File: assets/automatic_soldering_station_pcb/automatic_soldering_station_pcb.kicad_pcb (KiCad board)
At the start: 2 copper layers, 130 x 100 mm, 24 parts, among them J1 XY_MOS, J2 MAX6675, J3 MAX6675, J4 MAX6675

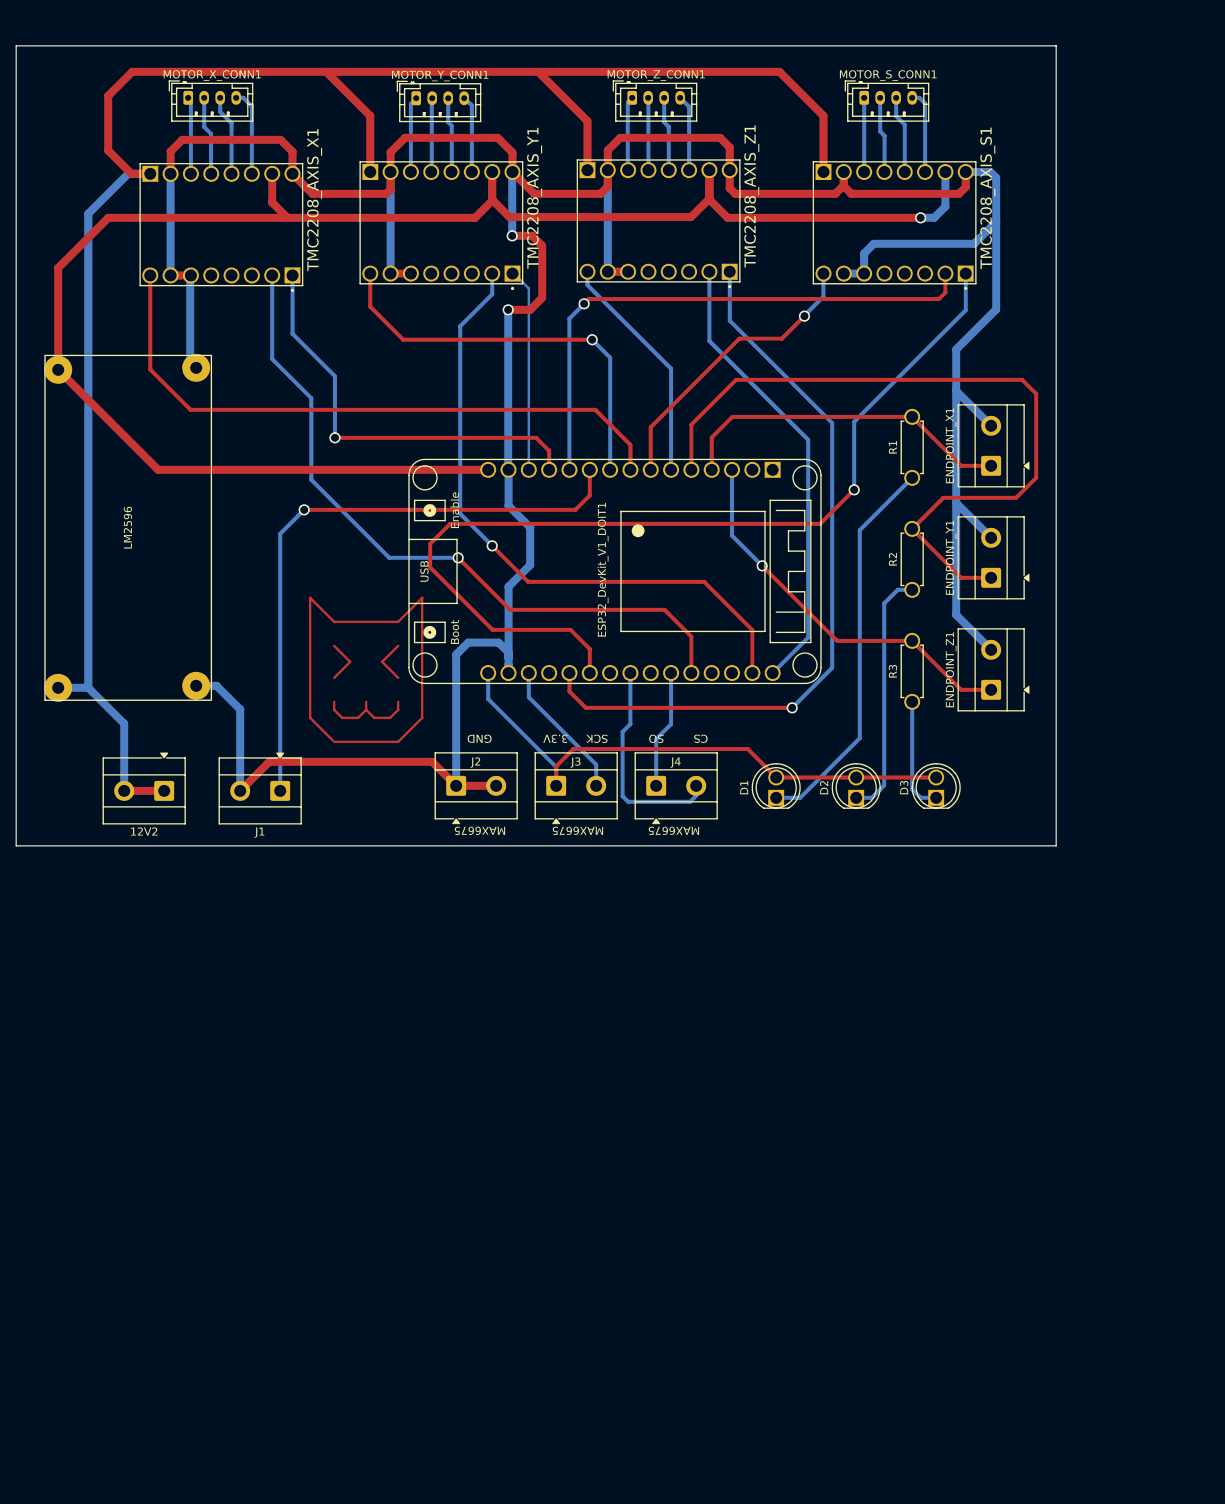
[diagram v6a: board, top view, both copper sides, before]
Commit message: pcb: update components placement and reduce pcb size
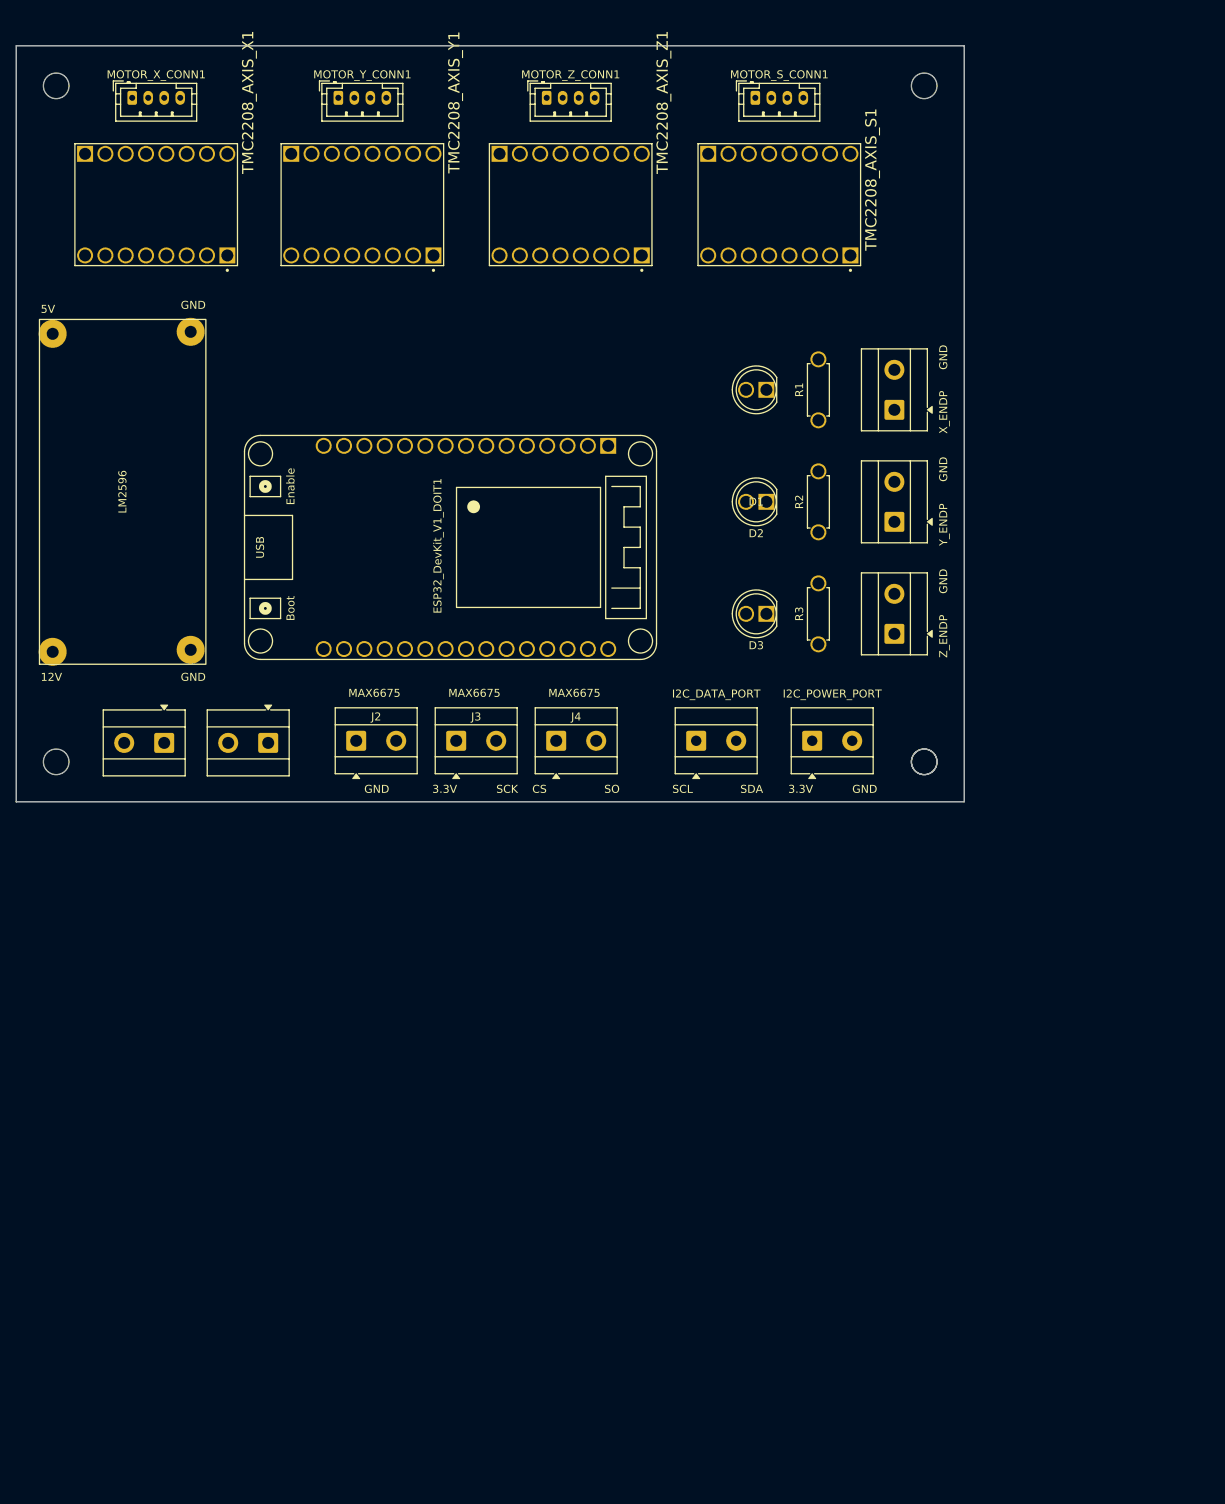
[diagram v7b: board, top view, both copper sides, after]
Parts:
- added ?: , , F.Cu at (125.5, 101.5)
- added ENDPOINT_Y2: I2C_POWER_PORT, TerminalBlock_MetzConnect:TerminalBlock_MetzConnect_Type055_RT01502HDWU_1x02_P5.00mm_Horizontal, F.Cu at (111.5, 98.9)
- added H1: MountingHole_3.2mm_M3, MountingHole:MountingHole_3.2mm_M3, F.Cu at (17.0, 17.0)
- added H2: MountingHole_3.2mm_M3, MountingHole:MountingHole_3.2mm_M3, F.Cu at (125.5, 17.0)
- added H3: MountingHole_3.2mm_M3, MountingHole:MountingHole_3.2mm_M3, F.Cu at (17.0, 101.5)
- added H4: MountingHole_3.2mm_M3, MountingHole:MountingHole_3.2mm_M3, F.Cu at (125.5, 101.5)
- added J5: I2C_DATA_PORT, TerminalBlock_MetzConnect:TerminalBlock_MetzConnect_Type055_RT01502HDWU_1x02_P5.00mm_Horizontal, F.Cu at (97.0, 98.9)
- moved D1 51.0 mm to (105.8, 55.0), turned to 180 degrees
- moved D2 38.7 mm to (105.8, 69.0), turned to 180 degrees
- moved D3 31.3 mm to (105.8, 83.0), turned to 180 degrees
- moved ESP32_DevKit_V1_DOIT1 20.8 mm to (86.0, 74.7)
- moved TMC2208_AXIS_S1 14.6 mm to (107.4, 31.9)
- moved ENDPOINT_X1 14.0 mm to (121.8, 57.5)
- moved ENDPOINT_Y1 14.0 mm to (121.8, 71.5)
- moved ENDPOINT_Z1 14.0 mm to (121.8, 85.5)
- moved R1 13.8 mm to (112.3, 58.8)
- moved R2 13.8 mm to (112.3, 72.8)
- moved R3 13.8 mm to (112.3, 86.8)
- moved J2 13.7 mm to (54.5, 98.9)
- moved J3 13.7 mm to (67.0, 98.9)
- moved J4 13.7 mm to (79.5, 98.9)
- moved MOTOR_S_CONN1 13.6 mm to (104.4, 18.5)
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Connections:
- ESP32_DevKit_V1_DOIT1 pad 22: unconnected-(ESP32_DevKit_V1_DOIT1-IO17-Pad22) -> /SCL
- ESP32_DevKit_V1_DOIT1 pad 24: unconnected-(ESP32_DevKit_V1_DOIT1-IO18-Pad24) -> /SDA
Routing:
- net GND: track 441.9 -> 0.00 mm, vias 2 -> 0
- net +12V: track 235.5 -> 0.00 mm
- net +5V: track 213.3 -> 0.00 mm, vias 1 -> 0
- net /S_DIR: track 118.7 -> 0.00 mm, vias 1 -> 0
- net /Z_DIR: track 92.9 -> 0.00 mm, vias 1 -> 0
- net /Y_ENDPOINT: track 92.8 -> 0.00 mm
- net /X_STEP: track 87.7 -> 0.00 mm, vias 1 -> 0
- net (no net): track 86.7 -> 0.00 mm
- net /Y_STEP: track 79.6 -> 0.00 mm, vias 1 -> 0
- net /X_EN: track 78.8 -> 0.00 mm
- net /XY_MOS_PWM: track 76.0 -> 0.00 mm, vias 1 -> 0
- net +3.3V: track 69.9 -> 0.00 mm
- net /S_STEP: track 69.6 -> 0.00 mm, vias 1 -> 0
- net /Z_STEP: track 57.1 -> 0.00 mm
- net /X_DIR: track 52.3 -> 0.00 mm, vias 1 -> 0
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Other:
- board size 130 x 100 mm -> 118.5 x 94.5 mm
- board text added: "12V"
- board text added: "5V"
- board text added: "SCL"
- board text added: "SDA"
- board text added: "X_ENDP"
- board text added: "Y_ENDP"
- board text added: "Z_ENDP"

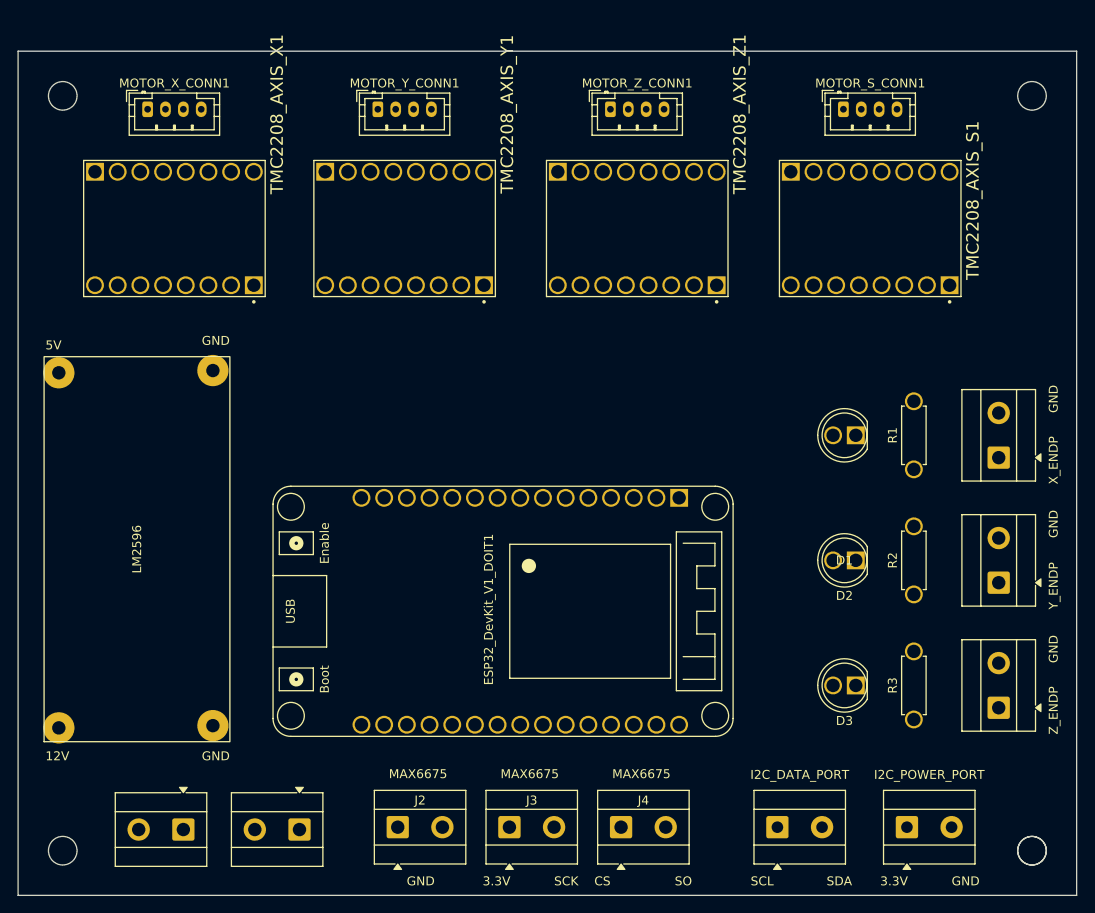
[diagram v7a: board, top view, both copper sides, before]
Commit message: pcb: change pcb for China manufacturing
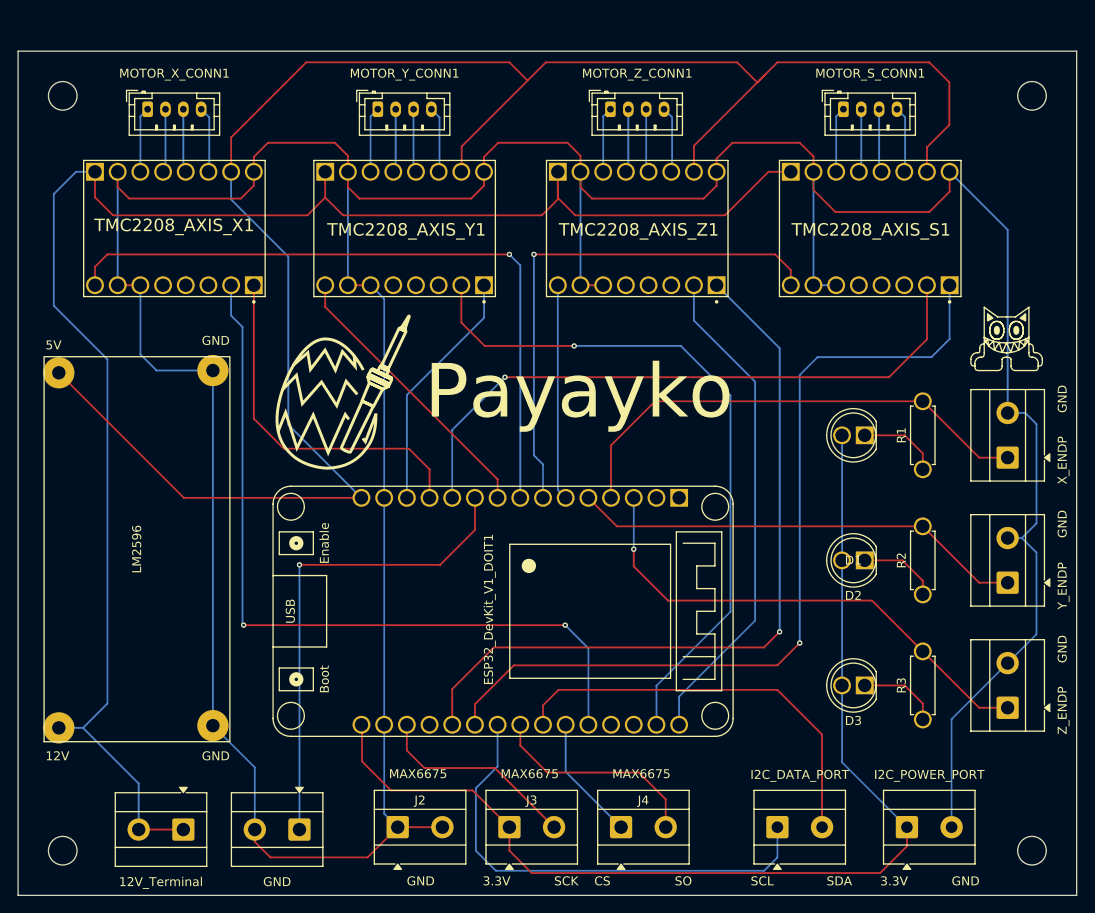
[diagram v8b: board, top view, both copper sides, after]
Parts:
- removed ?: , 
- moved D1 1.00 mm to (106.8, 55.0)
- moved D2 1.00 mm to (106.8, 69.0)
- moved D3 1.00 mm to (106.8, 83.0)
- moved ENDPOINT_X1 1.00 mm to (122.8, 57.5)
- moved ENDPOINT_Y1 1.00 mm to (122.8, 71.5)
- moved ENDPOINT_Z1 1.00 mm to (122.8, 85.5)
- moved R1 1.00 mm to (113.3, 58.8)
- moved R2 1.00 mm to (113.3, 72.8)
- moved R3 1.00 mm to (113.3, 86.8)
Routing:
- net GND: track 0.00 -> 430.7 mm
- net +5V: track 0.00 -> 213.1 mm
- net +12V: track 0.00 -> 185.1 mm
- net +3.3V: track 0.00 -> 122.1 mm
- net /S_DIR: track 0.00 -> 96.0 mm, vias 0 -> 1
- net /X_STEP: track 0.00 -> 86.9 mm, vias 0 -> 2
- net /Z_DIR: track 0.00 -> 85.0 mm, vias 0 -> 1
- net /Y_STEP: track 0.00 -> 78.0 mm, vias 0 -> 1
- net /X_EN: track 0.00 -> 76.8 mm, vias 0 -> 1
- net /S_STEP: track 0.00 -> 71.0 mm, vias 0 -> 1
- net /S_EN: track 0.00 -> 58.8 mm, vias 0 -> 1
- net /Z_ENDPOINT: track 0.00 -> 56.2 mm, vias 0 -> 1
- net /Z_STEP: track 0.00 -> 55.6 mm
- net /X_ENDPOINT: track 0.00 -> 54.9 mm
- net /XY_MOS_PWM: track 0.00 -> 54.5 mm, vias 0 -> 1
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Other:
- board text added: "Payayko"
